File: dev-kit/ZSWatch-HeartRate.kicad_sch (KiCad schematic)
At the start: 49 parts, among them IC101 LIS2DS12, IC102 MCP73832-2-OT, IC103 MAX32664, IC104 TPS61240, IC105 MAX86141, IC106 MIC5365-1.8, J101 SPI, J104 I2C, M101 BM15C, Q101 BSS138, SW101 BTN1, SW102 RESET, X102 CHARGE, X103 BATTERY, X104 DEBUG, Y101 32kHz

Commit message: Final check from Daniel before production
Signed-off-by: Daniel Kampert <DanielKampert@kampis-elektroecke.de>
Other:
- note added: "NOTE: Only this pins are working for I2C!"
- note added: "The hub firmware uses - LED1 for Green - LED2 for IR - LED3 for red"
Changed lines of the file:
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@@
 		(company "https://github.com/ZSWatch/Heartrate-HW")
 	)
+	(text "The hub firmware uses\n- LED1 for Green\n- LED2 for IR\n- LED3 for red"
+		(exclude_from_sim no)
+		(at 340.995 102.235 0)
+		(effects
+			(font
+				(size 1.27 1.27)
+			)
+			(justify left top)
+		)
+	)
+	(text "NOTE: Only this pins are working for I2C!"
+		(exclude_from_sim no)
+		(at 120.65 193.04 0)
+		(effects
+			(font
+				(size 1.27 1.27)
+			)
+			(justify left top)
+		)
+	)
 	(text "Layout guidelines for MAX8614x:\n- Connect all GNDs to a single ground plane and use one single via to PCB ground\n- Use different vias for all decoupling caps\n- PD_IN must be shielded by PD_GND\n- PD_GND on the layer where the MAX8614x is mounted, PG_IN under PD_GND\n- No traces over or under PD_GND"
 		(exclude_from_sim no)
@@
 			)
 		)
-		(property "Description" ""
+		(property "Description" "Power symbol creates a global label with name \"+1V8\""
 			(at 273.05 241.3 0)
 			(effects
@@
 			)
 		)
-		(property "Datasheet" "https://www.mouser.de/datasheet/2/447/KEM_C1002_X7R_SMD-3316098.pdf"
+		(property "Datasheet" "https://www.yageogroup.com/content/datasheet/asset/file/KEM_C1002_X7R_SMD"
 			(at 91.44 160.02 0)
 			(effects
@@
 			)
 		)
-		(property "Description" ""
+		(property "Description" "Power symbol creates a global label with name \"GND\" , ground"
 			(at 273.05 274.32 0)
 			(effects
@@
 			)
 		)
-		(property "Datasheet" "https://www.mouser.de/datasheet/2/40/cx5r_KGM-3223198.pdf"
+		(property "Datasheet" "https://www.mouser.de/datasheet/2/40/cx5r-2835979.pdf"
 			(at 176.53 105.41 0)
 			(effects
@@
 			)
 		)
-		(property "Datasheet" "https://www.mouser.de/datasheet/2/40/cx5r_KGM-3223198.pdf"
+		(property "Datasheet" "https://www.mouser.de/datasheet/2/40/cx5r-2835979.pdf"
 			(at 198.12 105.41 0)
 			(effects
@@
 			)
 		)
-		(property "Datasheet" "https://www.mouser.de/datasheet/2/40/cx5r_KGM-3223198.pdf"
+		(property "Datasheet" "https://www.mouser.de/datasheet/2/40/cx5r-2835979.pdf"
 			(at 187.96 105.41 0)
 			(effects
@@
 			)
 		)
-		(property "Description" ""
+		(property "Description" "Two pin crystal"
 			(at 168.91 148.59 0)
 			(effects
@@
 			)
 		)
-		(property "Datasheet" ""
+		(property "Datasheet" "~"
 			(at 391.16 231.14 0)
 			(effects
@@
 		(pin "D4"
 		)
-		(pin "D4"
-		)
 		(pin "A5"
 		)
@@
 			)
 		)
-		(property "Datasheet" "https://www.mouser.de/datasheet/2/268/MIC5365_6_High_Performance_Single_150mA_LDO_DS2000-3442271.pdf"
+		(property "Datasheet" "https://ww1.microchip.com/downloads/en/DeviceDoc/mic5365.pdf"
 			(at 377.19 72.39 0)
 			(effects
@@
 			)
 		)
-		(property "Datasheet" "https://www.mouser.de/datasheet/2/447/KEM_C1002_X7R_SMD-3316098.pdf"
+		(property "Datasheet" "https://www.yageogroup.com/content/datasheet/asset/file/KEM_C1002_X7R_SMD"
 			(at 299.72 96.52 0)
 			(effects
@@
 			)
 		)
-		(property "Datasheet" ""
+		(property "Datasheet" "~"
 			(at 391.16 234.95 0)
 			(effects
@@
 			)
 		)
-		(property "Description" ""
+		(property "Description" "Power symbol creates a global label with name \"GND\" , ground"
 			(at 297.18 228.6 0)
 			(effects
@@
 			)
 		)
-		(property "Description" ""
+		(property "Description" "Power symbol creates a global label with name \"GND\" , ground"
 			(at 87.63 251.46 0)
 			(effects
@@
 			)
 		)
-		(property "Datasheet" "https://www.mouser.de/datasheet/2/40/cx5r_KGM-3223198.pdf"
+		(property "Datasheet" "https://www.mouser.de/datasheet/2/40/cx5r-2835979.pdf"
 			(at 285.75 96.52 0)
 			(effects
@@
 			)
 		)
-		(property "Datasheet" "https://www.molex.com/en-us/products/part-detail/781710002?display=pdf"
+		(property "Datasheet" "https://www.molex.com/en-us/products/part-detail-pdf/781710002?display=pdf"
 			(at 298.45 22.86 0)
 			(effects
@@
 			)
 		)
-		(property "Description" ""
+		(property "Description" "Power symbol creates a global label with name \"+1V8\""
 			(at 297.18 182.88 0)
 			(effects
@@
 			)
 		)
-		(property "Datasheet" "https://www.mouser.de/datasheet/2/447/KEM_C1002_X7R_SMD-3316098.pdf"
+		(property "Datasheet" "https://www.yageogroup.com/content/datasheet/asset/file/KEM_C1002_X7R_SMD"
 			(at 302.26 187.96 0)
 			(effects
@@
 			)
 		)
-		(property "Description" ""
+		(property "Description" "Cortex Debug Connector, standard ARM Cortex-M SWD and JTAG interface"
 			(at 273.05 257.81 0)
 			(effects
@@
 			)
 		)
+		(property "Sim.Pins" "1=K 2=A"
+			(at 43.18 224.79 0)
+			(effects
+				(font
+					(size 1.27 1.27)
+				)
+				(hide yes)
+			)
+		)
 		(pin "1"
 		)
@@
 			)
 		)
-		(property "Datasheet" "https://www.mouser.de/datasheet/2/447/KEM_C1002_X7R_SMD-3316098.pdf"
+		(property "Datasheet" "https://www.yageogroup.com/content/datasheet/asset/file/KEM_C1002_X7R_SMD"
 			(at 289.56 187.96 0)
 			(effects
@@
 			)
 		)
-		(property "Datasheet" "https://www.mouser.de/datasheet/2/40/cx5r_KGM-3223198.pdf"
+		(property "Datasheet" "https://www.mouser.de/datasheet/2/40/cx5r-2835979.pdf"
 			(at 355.6 40.64 0)
 			(effects
@@
 			)
 		)
-		(property "Description" ""
+		(property "Description" "Power symbol creates a global label with name \"GND\" , ground"
 			(at 317.5 228.6 0)
 			(effects
@@
 			)
 		)
-		(property "Datasheet" "https://www.mouser.de/datasheet/2/609/MAX32664-3469756.pdf"
+		(property "Datasheet" "https://www.analog.com/media/en/technical-documentation/data-sheets/MAX32664.pdf"
 			(at 193.04 135.89 0)
 			(effects

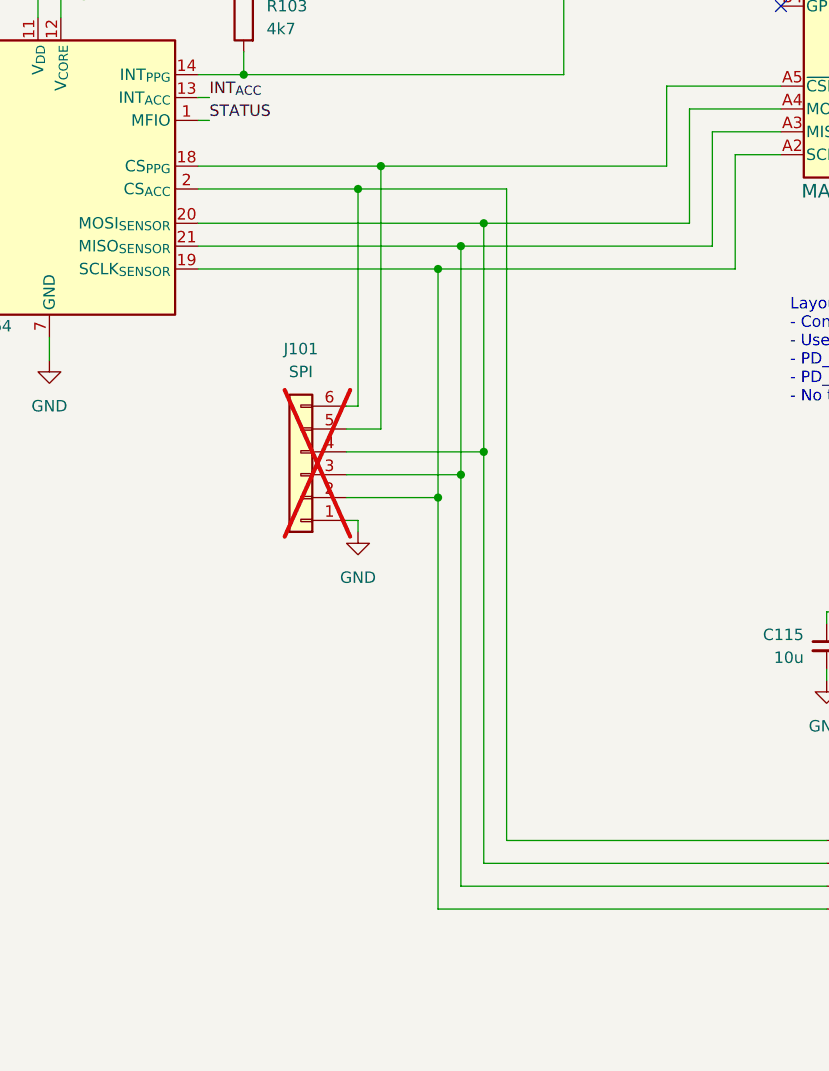
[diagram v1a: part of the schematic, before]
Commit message: Add MFIO to SPI header
Signed-off-by: Daniel Kampert <DanielKampert@kampis-elektroecke.de>
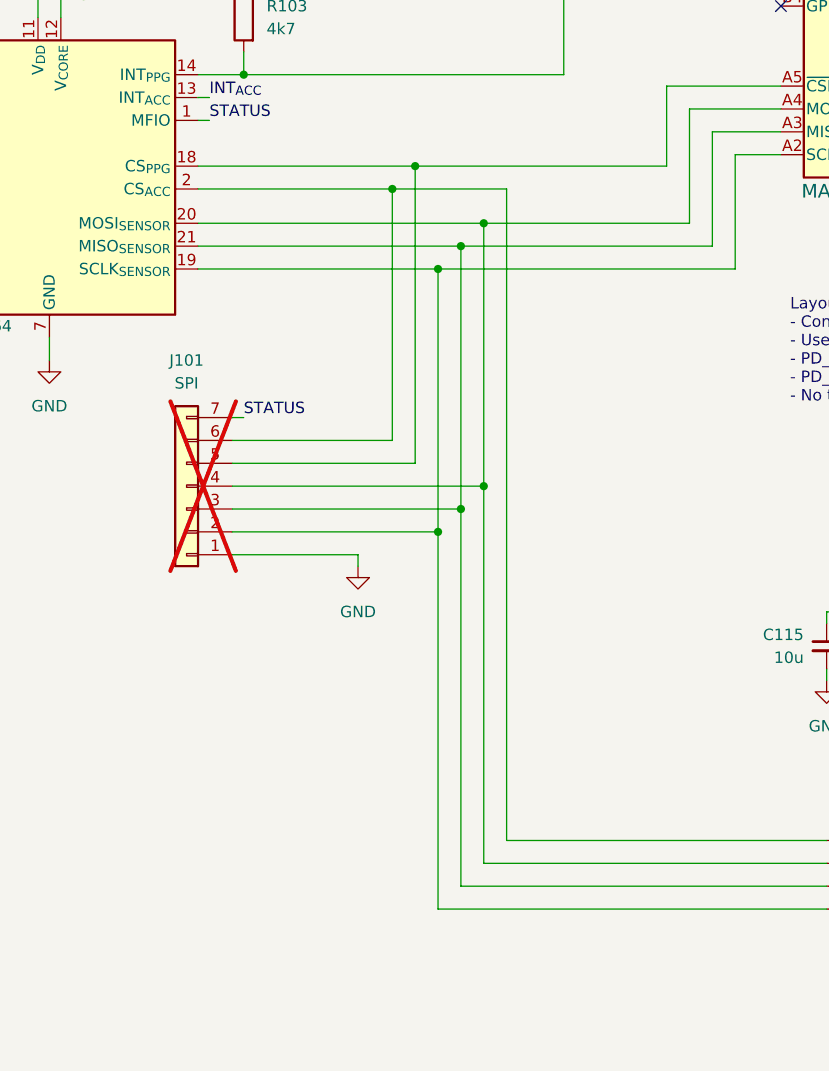
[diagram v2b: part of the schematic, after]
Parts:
- J101: footprint Connector_PinHeader_2.54mm:PinHeader_1x06_P2.54mm_Vertical -> Connector_PinHeader_2.54mm:PinHeader_1x07_P2.54mm_Vertical; symbol Connector_Generic:Conn_01x06 -> Connector_Generic:Conn_01x07
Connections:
- net STATUS: now also J101.7 (Pin_7)
